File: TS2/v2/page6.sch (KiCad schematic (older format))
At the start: 23 parts, among them SW2 SINGLE STEP/RUN, SW3 STEP, U10 74LS32, U19 74LS20, U20 74LS74, U21 74LS161, U22 74LS161, U23 74LS74, U4 74LS06, U5 74LS04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

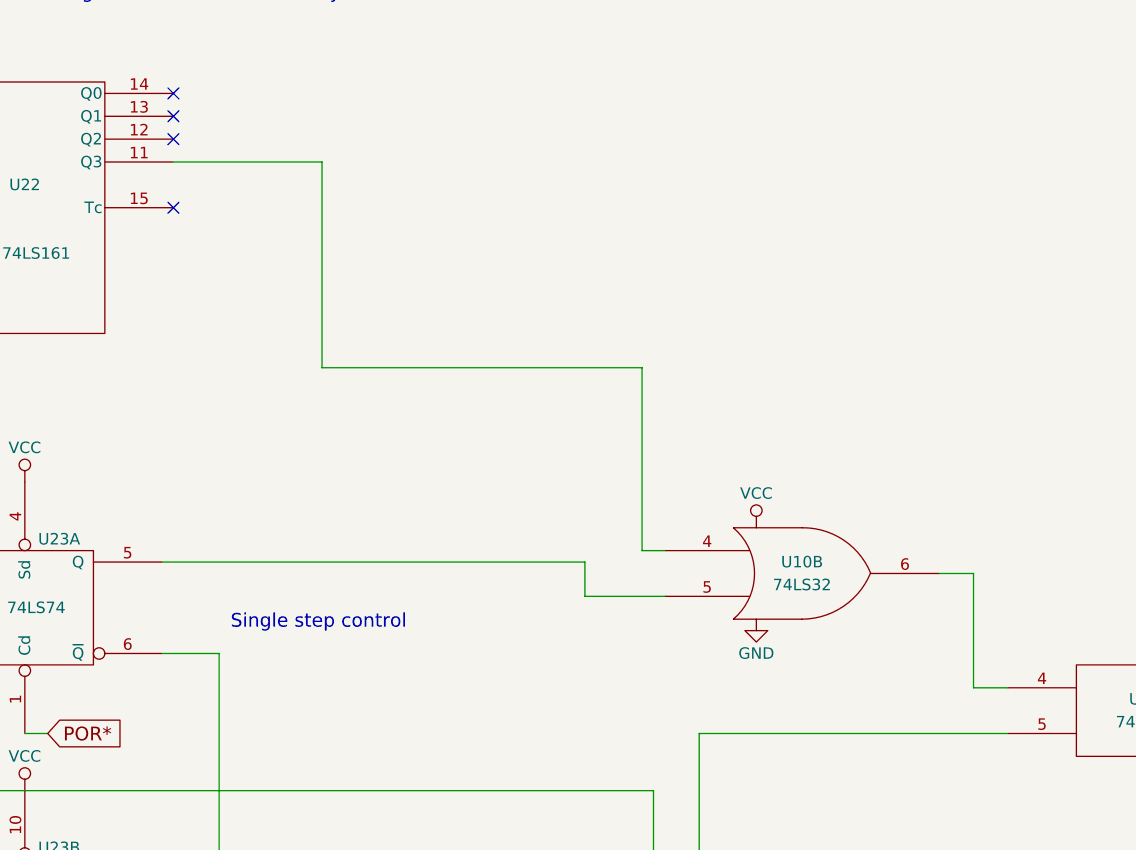
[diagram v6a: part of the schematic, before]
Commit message: Route some wires better.
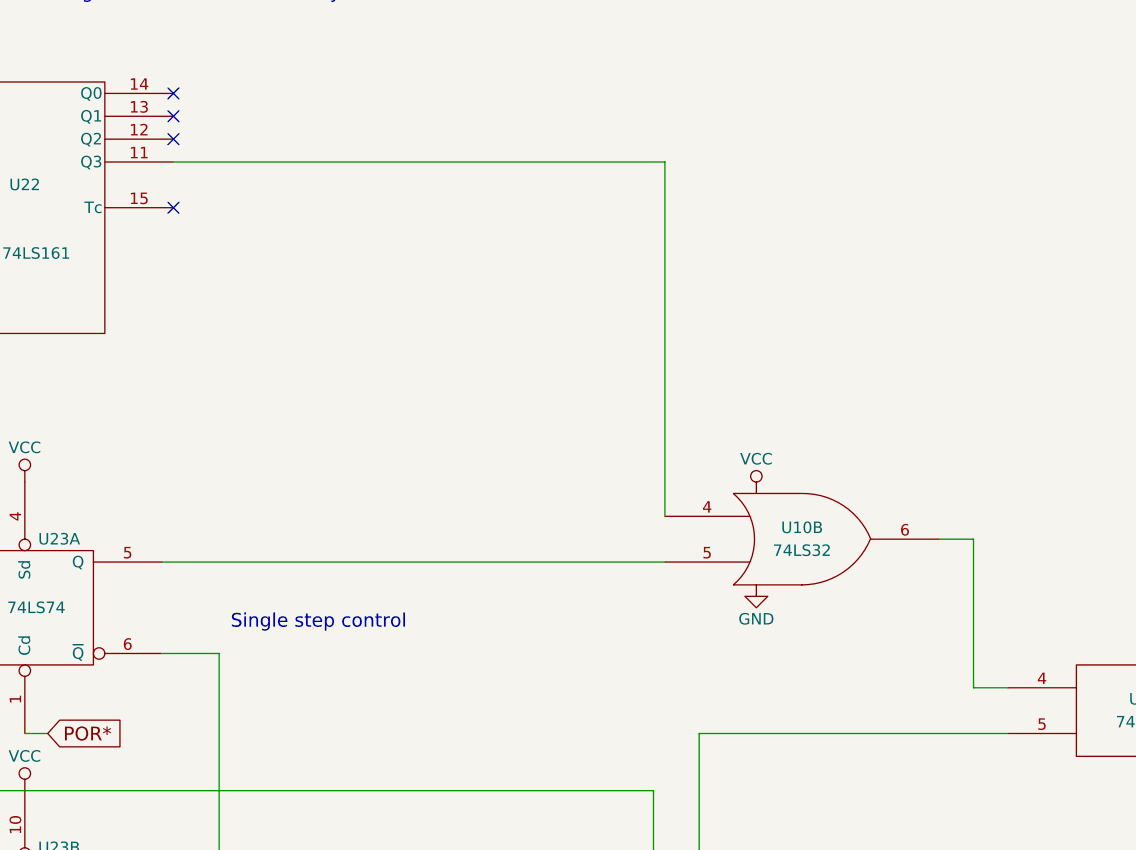
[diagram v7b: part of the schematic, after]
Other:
- moved on the sheet: U10B
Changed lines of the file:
@@
 L 74LS32 U10
 U 2 1 57CB85C1
-P 7850 3400
-F 0 "U10" H 7850 3450 50  0000 C CNN
-F 1 "74LS32" H 7850 3350 50  0000 C CNN
-F 2 "" H 7850 3400 50  0000 C CNN
-F 3 "" H 7850 3400 50  0000 C CNN
-	2    7850 3400
+P 7850 3250
+F 0 "U10" H 7850 3300 50  0000 C CNN
+F 1 "74LS32" H 7850 3200 50  0000 C CNN
+F 2 "" H 7850 3250 50  0000 C CNN
+F 3 "" H 7850 3250 50  0000 C CNN
+	2    7850 3250
 	1    0    0    -1
 $EndComp
@@
 	3100 2100 3700 2100
 Wire Wire Line
-	5100 1600 5750 1600
-Wire Wire Line
-	5750 1600 5750 2500
-Wire Wire Line
-	5750 2500 7150 2500
-Wire Wire Line
-	7150 2500 7150 3300
-Wire Wire Line
-	7150 3300 7250 3300
-Wire Wire Line
-	8450 3400 8600 3400
-Wire Wire Line
-	8600 3400 8600 3900
+	5100 1600 7250 1600
+Wire Wire Line
+	8600 3250 8600 3900
 Wire Wire Line
 	8600 3900 8750 3900
@@
 $EndComp
 Wire Wire Line
-	5050 3350 6900 3350
-Wire Wire Line
-	6900 3350 6900 3500
-Wire Wire Line
-	6900 3500 7250 3500
+	5050 3350 7250 3350
 Wire Wire Line
 	3850 3550 3850 4350
@@
 L GND #PWR084
 U 1 1 57CB624C
-P 7650 3600
-F 0 "#PWR084" H 7650 3350 50  0001 C CNN
-F 1 "GND" H 7650 3450 50  0000 C CNN
-F 2 "" H 7650 3600 50  0000 C CNN
-F 3 "" H 7650 3600 50  0000 C CNN
-	1    7650 3600
+P 7650 3450
+F 0 "#PWR084" H 7650 3200 50  0001 C CNN
+F 1 "GND" H 7650 3300 50  0000 C CNN
+F 2 "" H 7650 3450 50  0000 C CNN
+F 3 "" H 7650 3450 50  0000 C CNN
+	1    7650 3450
 	1    0    0    -1
 $EndComp
@@
 L VCC #PWR085
 U 1 1 57CB85E0
-P 7650 3200
-F 0 "#PWR085" H 7650 3050 50  0001 C CNN
-F 1 "VCC" H 7650 3350 50  0000 C CNN
-F 2 "" H 7650 3200 50  0000 C CNN
-F 3 "" H 7650 3200 50  0000 C CNN
-	1    7650 3200
+P 7650 3050
+F 0 "#PWR085" H 7650 2900 50  0001 C CNN
+F 1 "VCC" H 7650 3200 50  0000 C CNN
+F 2 "" H 7650 3050 50  0000 C CNN
+F 3 "" H 7650 3050 50  0000 C CNN
+	1    7650 3050
 	1    0    0    -1
 $EndComp
@@
 Text Notes 4350 900  0    60   ~ 0
 DTACK* generator for local memory
+Wire Wire Line
+	7250 1600 7250 3150
+Wire Wire Line
+	8450 3250 8600 3250
 $EndSCHEMATC
